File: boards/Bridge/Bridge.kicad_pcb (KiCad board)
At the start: 2 copper layers, 50 x 50 mm, 32 parts, among them CN1 PinHeader, CN2 PinSocket, CN3 PinHeader, CN4 PinHeader, CN5 PinHeader, CN6 Grove, CN7 Grove, CN8 Grove, U1 74LVC2G125, U2 74HCT2G125, U3 PCA9685PW

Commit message: modify PCB design
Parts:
- CN7, CN8: footprint Connector_JST:JST_PH_B4B-PH-K_1x04_P2.00mm_Vertical -> Grove:GROVE-HW4-2.0
- moved CN7 3.00 mm to (133.0, 55.0), turned to 0 degrees
- moved CN8 3.00 mm to (119.5, 55.0), turned to 0 degrees
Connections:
- CN7 pad 1: GND -> /ADC
- CN7 pad 2: +5V -> /DAC
- CN7 pad 3: /DAC -> +5V
- CN7 pad 4: /ADC -> GND
- CN8 pad 1: GND -> /RXD2
- CN8 pad 2: +5V -> /TXD2
- CN8 pad 3: /TXD2 -> +5V
- CN8 pad 4: /RXD2 -> GND
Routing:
- net +5VM: track 50.4 -> 51.9 mm

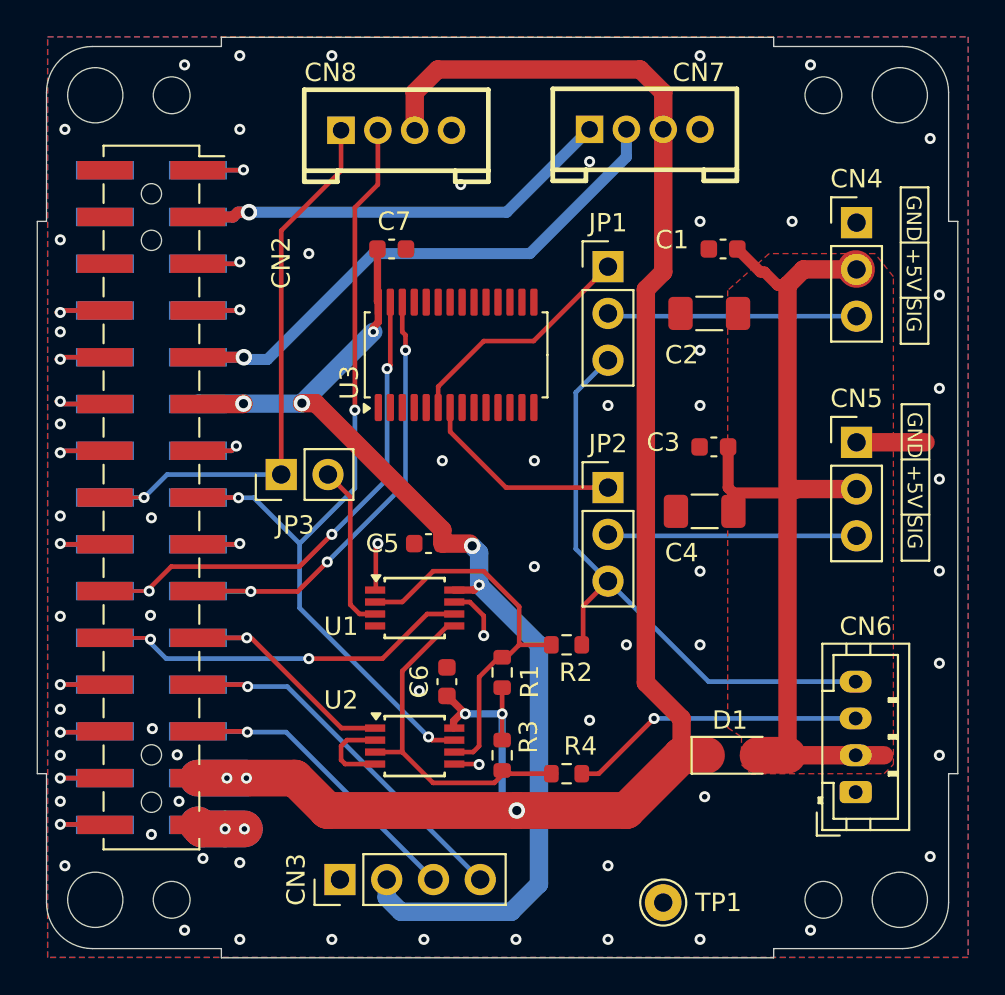
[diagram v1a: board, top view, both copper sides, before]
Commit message: modify PCB design for DRC
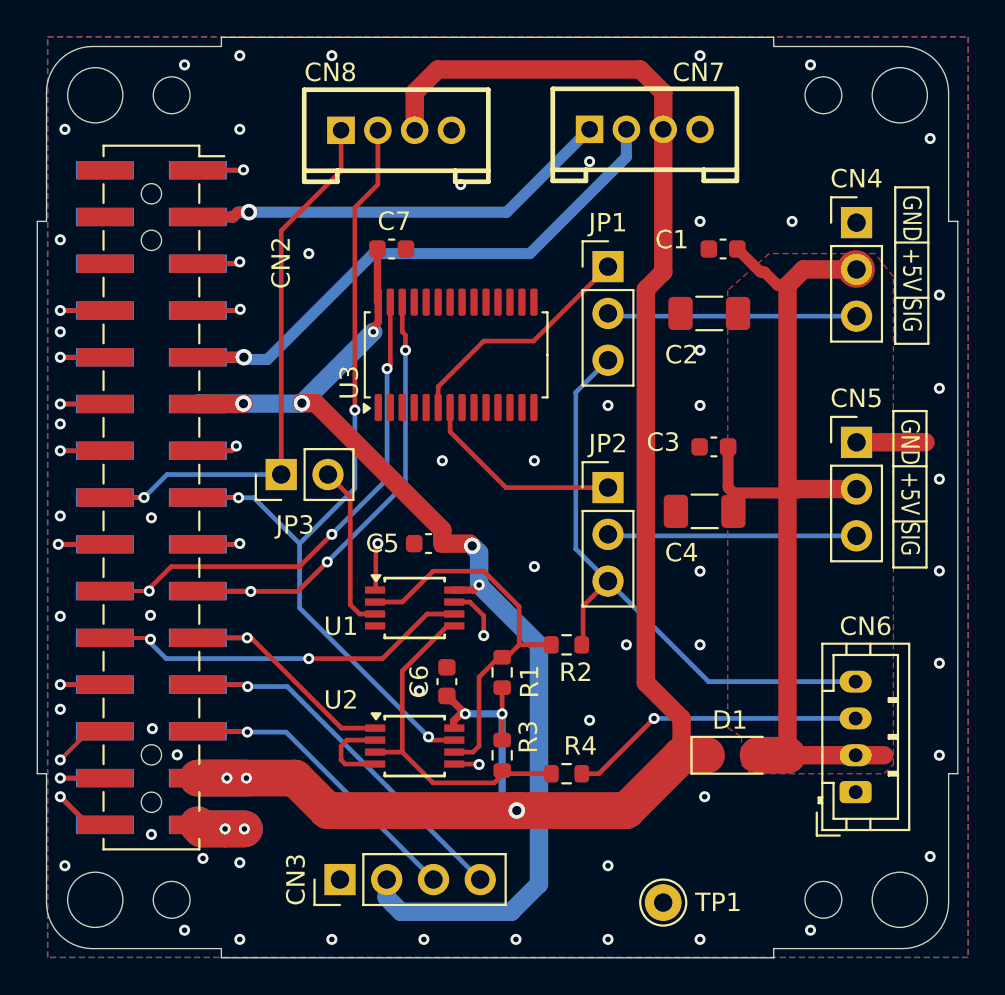
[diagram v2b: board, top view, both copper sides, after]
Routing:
- net /PIN26: track 4.40 -> 6.28 mm
- net /PIN30: track 4.88 -> 6.53 mm
- net /PIN12: track 5.44 -> 4.86 mm
- net /PIN14: track 5.41 -> 4.86 mm
- net GND: vias 61 -> 58

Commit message: fix PCB design
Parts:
- CN6: footprint Connector_JST:JST_PH_B4B-PH-K_1x04_P2.00mm_Vertical -> Grove:GROVE-HW4-2.0
- moved CN6 3.00 mm to (144.4, 88.0), turned to -90 degrees
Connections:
- CN6 pad 1: GND -> /SERIAL1
- CN6 pad 2: +5VM -> /SERIAL2
- CN6 pad 3: /SERIAL2 -> +5VM
- CN6 pad 4: /SERIAL1 -> GND

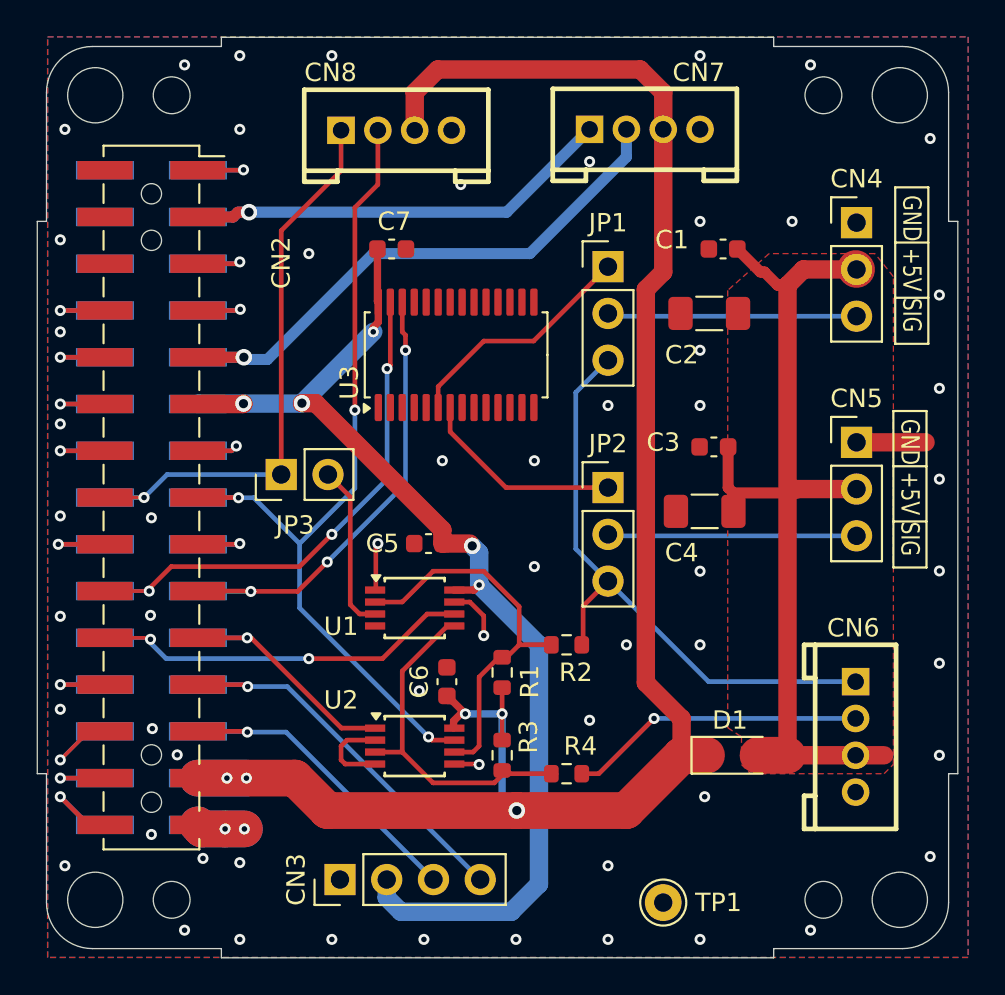
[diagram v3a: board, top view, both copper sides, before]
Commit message: fix PCB design (product ver1.0)
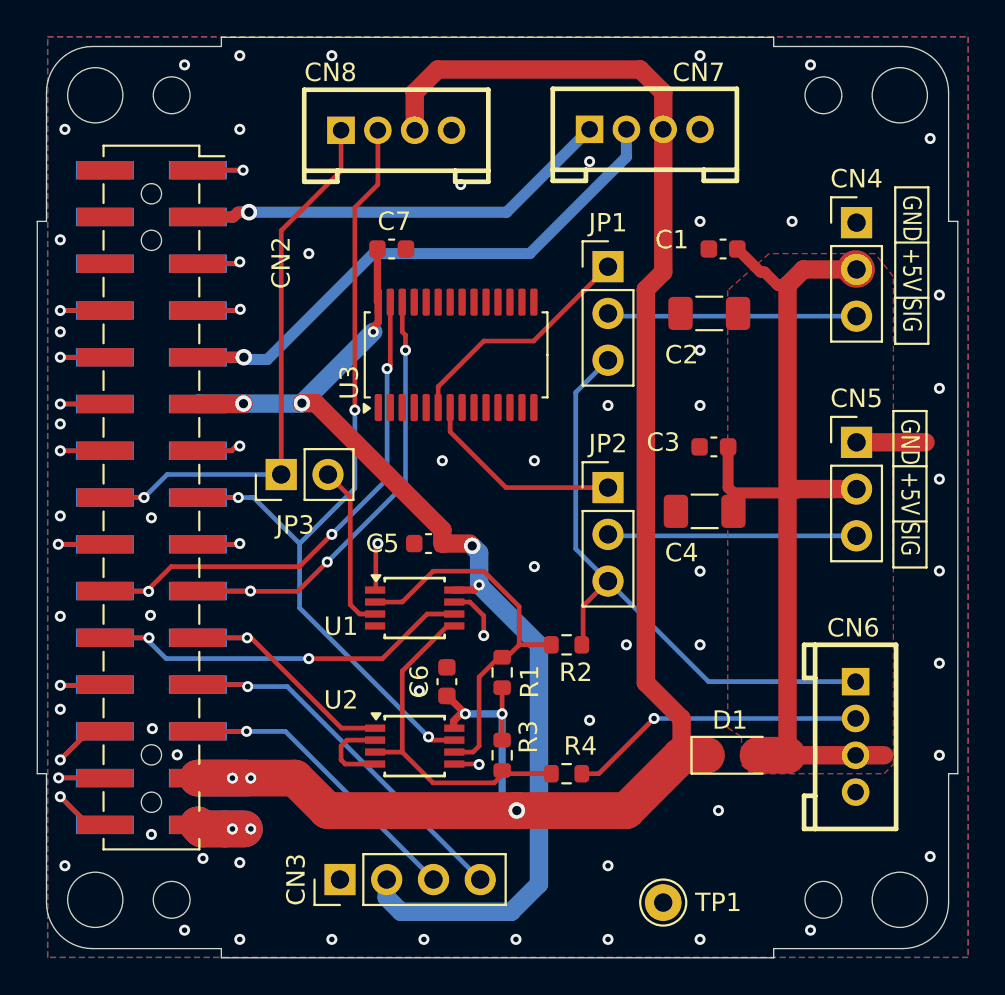
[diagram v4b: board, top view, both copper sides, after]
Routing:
- net /RXD2: track 32.9 -> 32.2 mm

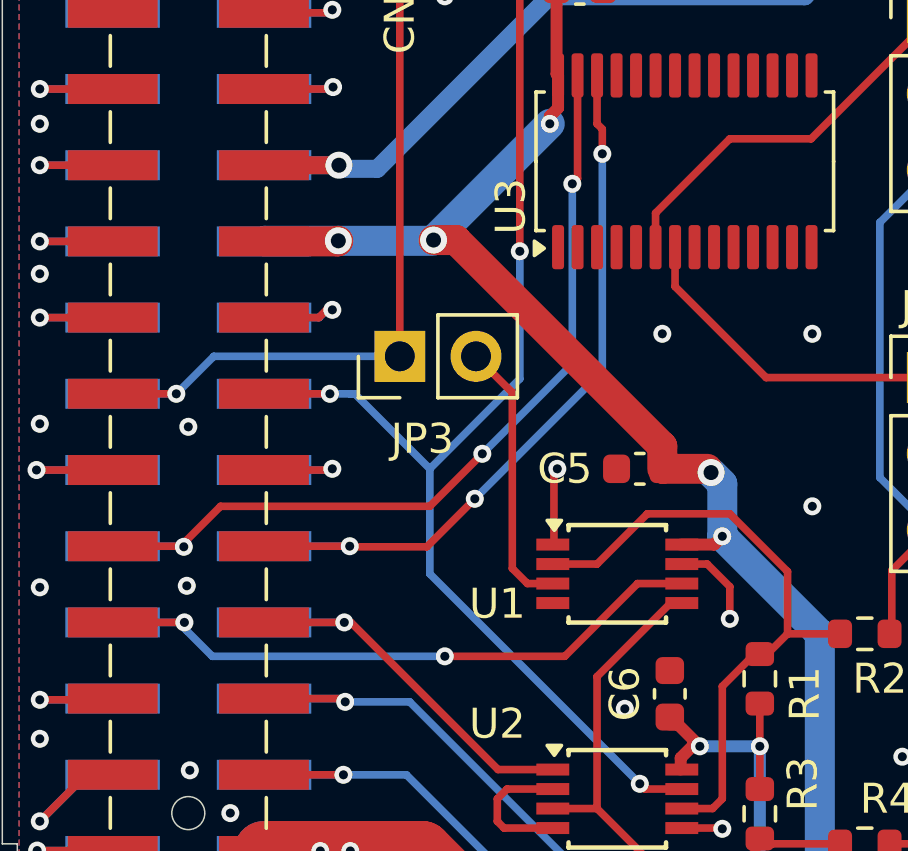
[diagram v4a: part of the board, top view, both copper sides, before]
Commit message: fix Bridge Board (add pull up resistors)
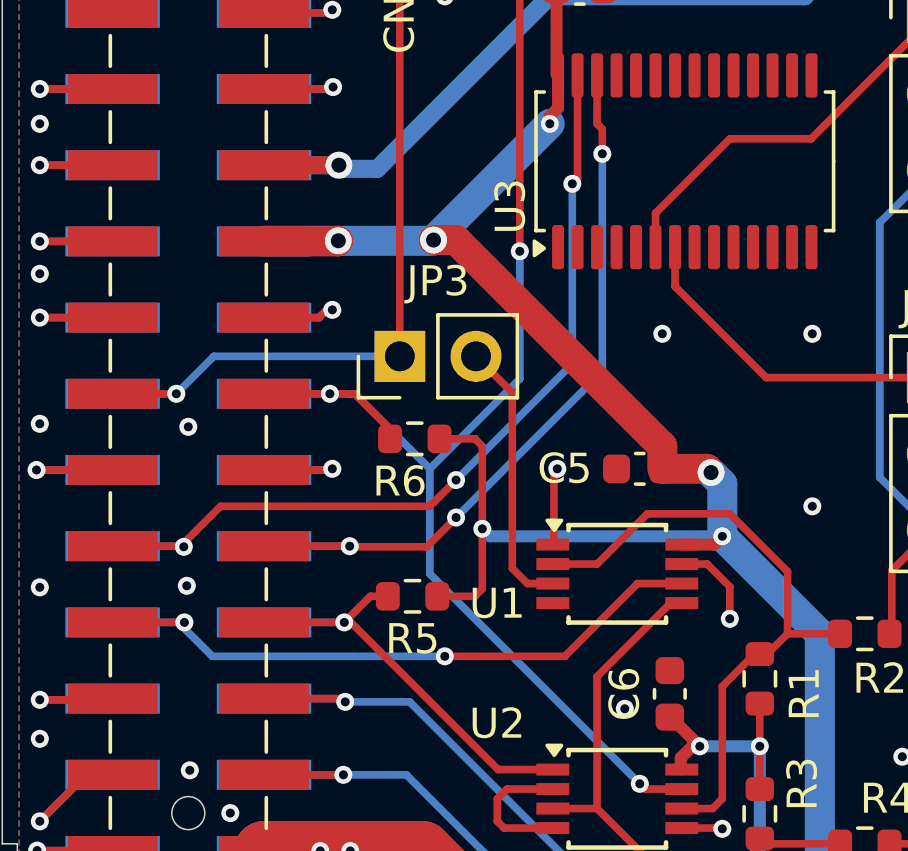
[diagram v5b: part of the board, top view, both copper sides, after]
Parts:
- added R5: 1k, Resistor_SMD:R_0603_1608Metric, F.Cu at (113.7, 81.8)
- added R6: 1k, Resistor_SMD:R_0603_1608Metric, F.Cu at (113.8, 76.5)
- CN4, CN5: value PinHeader -> B3B-EH-A
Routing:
- net +3V3: track 62.3 -> 78.3 mm, vias 5 -> 6
- net /TXD2: track 47.8 -> 50.6 mm
- net /TXD1: track 14.4 -> 16.2 mm
